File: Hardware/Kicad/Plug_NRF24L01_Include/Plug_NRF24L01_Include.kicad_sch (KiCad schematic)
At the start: 43 parts, among them J1 Conn_01x07_Socket, Q1 2N7002, Q2 2N7002, Q3 2N7002, SW1 SW_Push, U1 NRF24L01, U2 AMS1117-3.3, U3 STM32L412KBTx, Y1 16 MHz

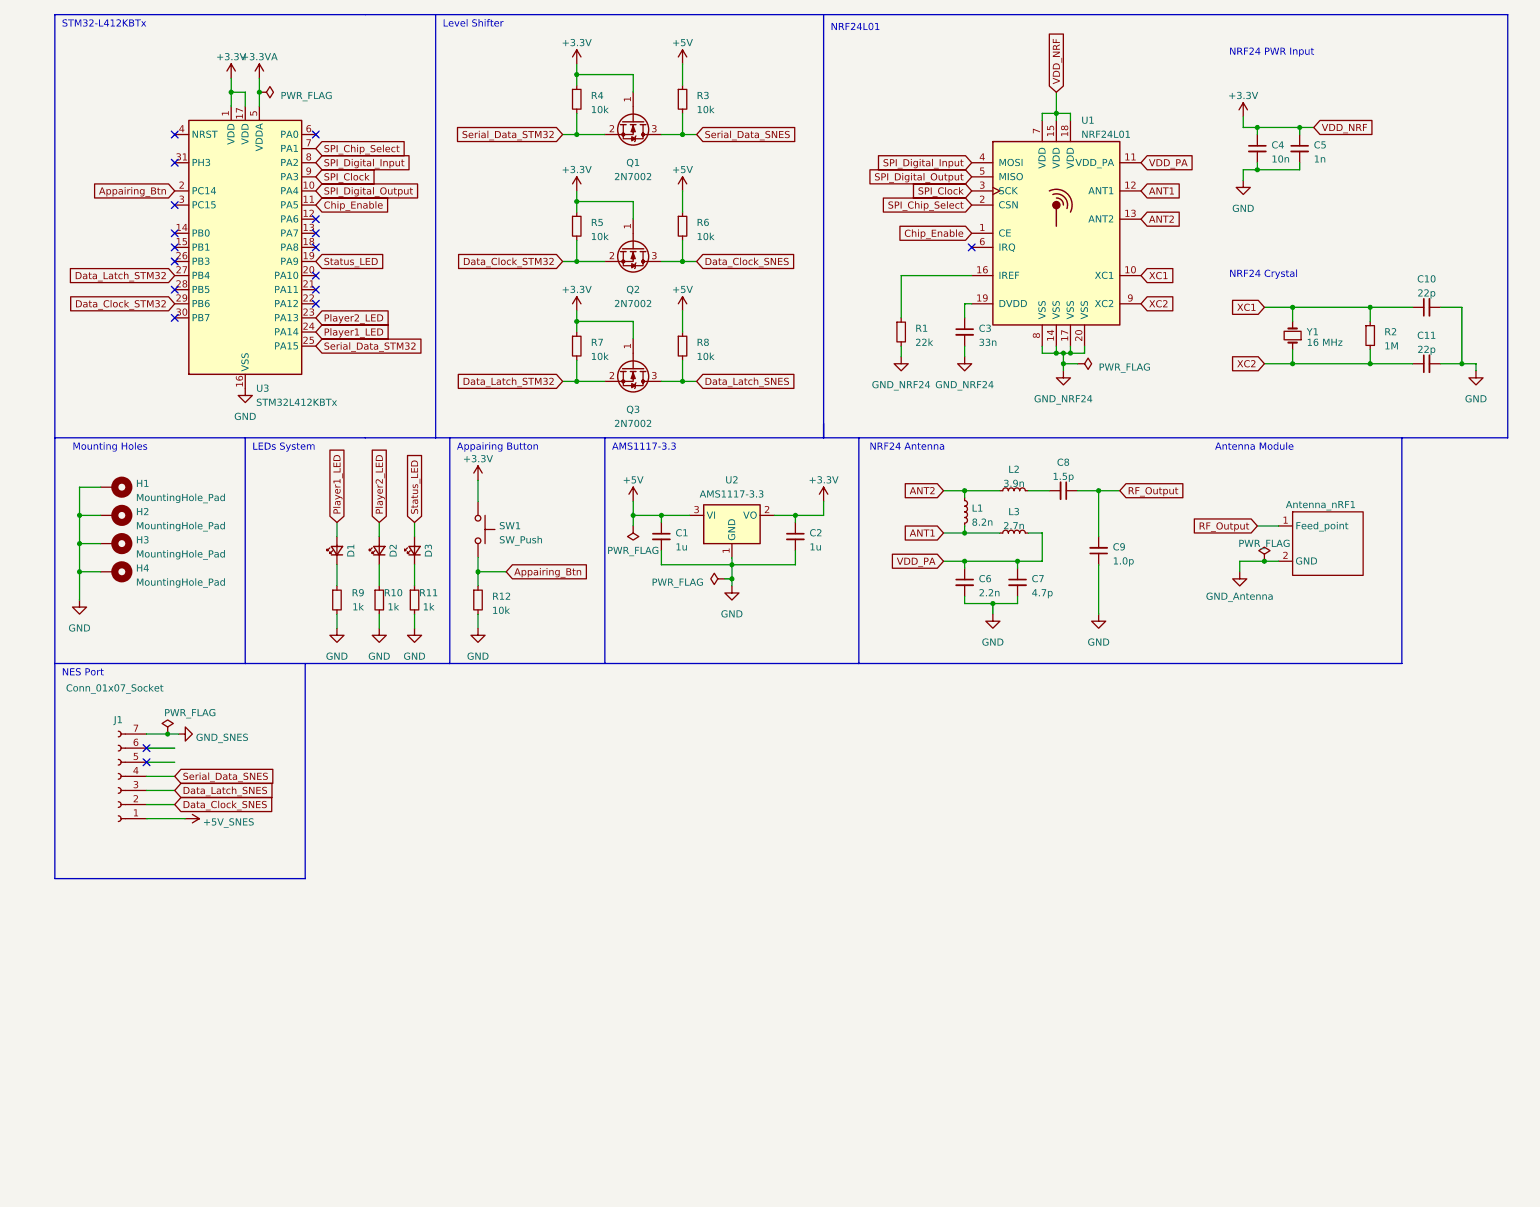
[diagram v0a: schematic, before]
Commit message: Updated NRF24L01_Include
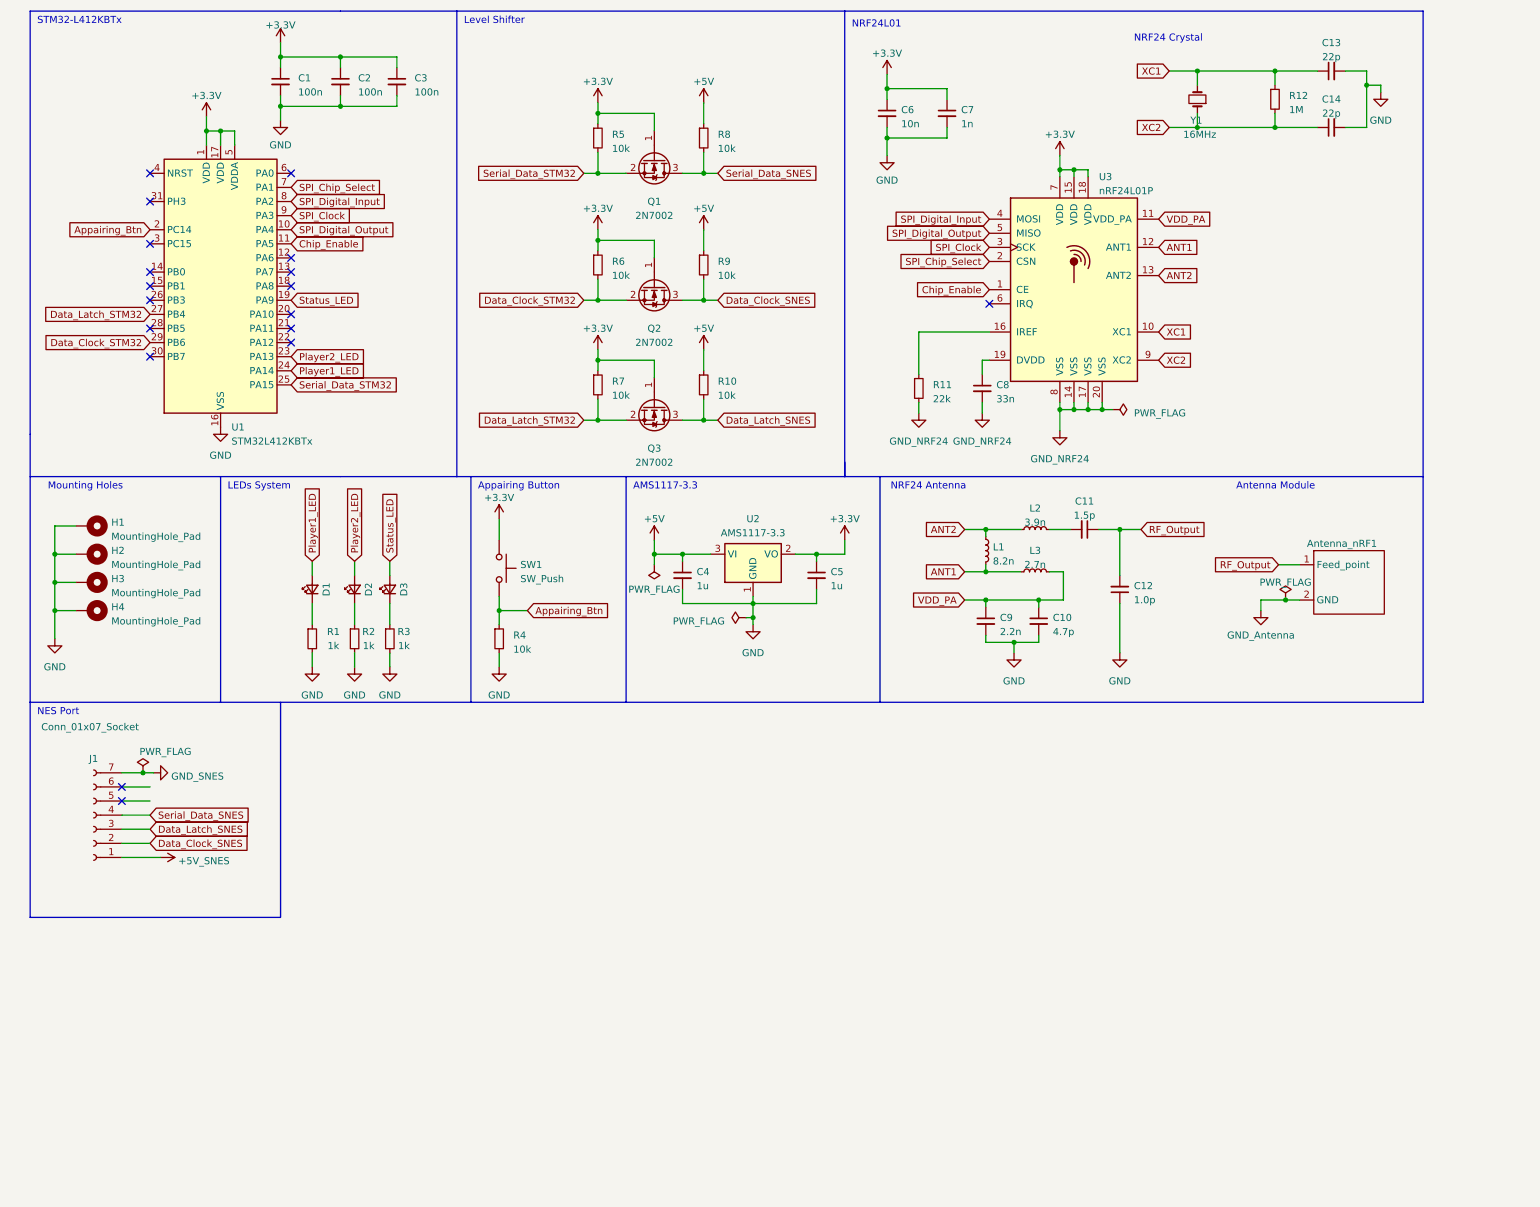
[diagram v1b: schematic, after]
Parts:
- removed C4: 10n, Capacitor_SMD:C_0603_1608Metric_Pad1.08x0.95mm_HandSolder, symbol Device:C_Small
- removed C5: 1n, Capacitor_SMD:C_0603_1608Metric_Pad1.08x0.95mm_HandSolder, symbol Device:C_Small
- removed U1: NRF24L01, Package_DFN_QFN:QFN-20-1EP_4x4mm_P0.5mm_EP2.5x2.5mm, symbol RF:NRF24L01
- added C1, C2, C3: 100n, Capacitor_SMD:C_0603_1608Metric_Pad1.08x0.95mm_HandSolder, symbol Device:C_Small
- added C6: 10n, Capacitor_SMD:C_0603_1608Metric_Pad1.08x0.95mm_HandSolder, symbol Device:C_Small
- added C7: 1n, Capacitor_SMD:C_0603_1608Metric_Pad1.08x0.95mm_HandSolder, symbol Device:C_Small
- added U3: nRF24L01P, Package_DFN_QFN:QFN-20-1EP_4x4mm_P0.5mm_EP2.5x2.5mm, symbol RF:nRF24L01P
- Y1: value 16 MHz -> 16MHz; footprint Crystal:Crystal_HC49-U_Horizontal -> Crystal:Crystal_SMD_HC49-SD_HandSoldering
- renumbered C7 to C10, C8 to C11, C9 to C12, C10 to C13, C11 to C14, C1 to C4, C2 to C5, C3 to C8, C6 to C9, R9 to R1, R8 to R10, R1 to R11, R2 to R12, R10 to R2, R11 to R3, R12 to R4, R4 to R5, R5 to R6, R3 to R8, R6 to R9, U3 to U1
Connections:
- net +3.3VA is gone; now on net +3.3V: U1.5 (VDDA)
- net +3.3V: now also C1.1, C2.1, C3.1, C6.1, C7.1, U3.15 (VDD), U3.18 (VDD), U3.7 (VDD)
- net ANT1: now also U3.12 (ANT1)
- net ANT2: now also U3.13 (ANT2)
- net Chip_Enable: now also U3.1 (CE)
- net GND: now also C1.2, C2.2, C3.2, C6.2, C7.2
- net GND1: now also U3.14 (VSS), U3.17 (VSS), U3.20 (VSS), U3.8 (VSS)
- net SPI_Chip_Select: now also U3.2 (CSN)
- net SPI_Clock: now also U3.3 (SCK)
- net SPI_Digital_Input: now also U3.4 (MOSI)
- net SPI_Digital_Output: now also U3.5 (MISO)
- net VDD_PA: now also U3.11 (VDD_PA)
- net XC1: now also U3.10 (XC1)
- net XC2: now also U3.9 (XC2)
- net at C8.1: now also U3.19 (DVDD)
- net at R11.1: now also U3.16 (IREF)
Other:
- note removed: "NRF24 PWR Input"
- moved on the sheet: Antenna_nRF1, C10, C11, C12, C13, C14, C4, C5, C8, C9, D1, D2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

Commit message: Updated Plug_NRF24L01_Include Schematic & Include (Added new components and modified footprints). Fixed some errors on NRF24L01_Exclude.
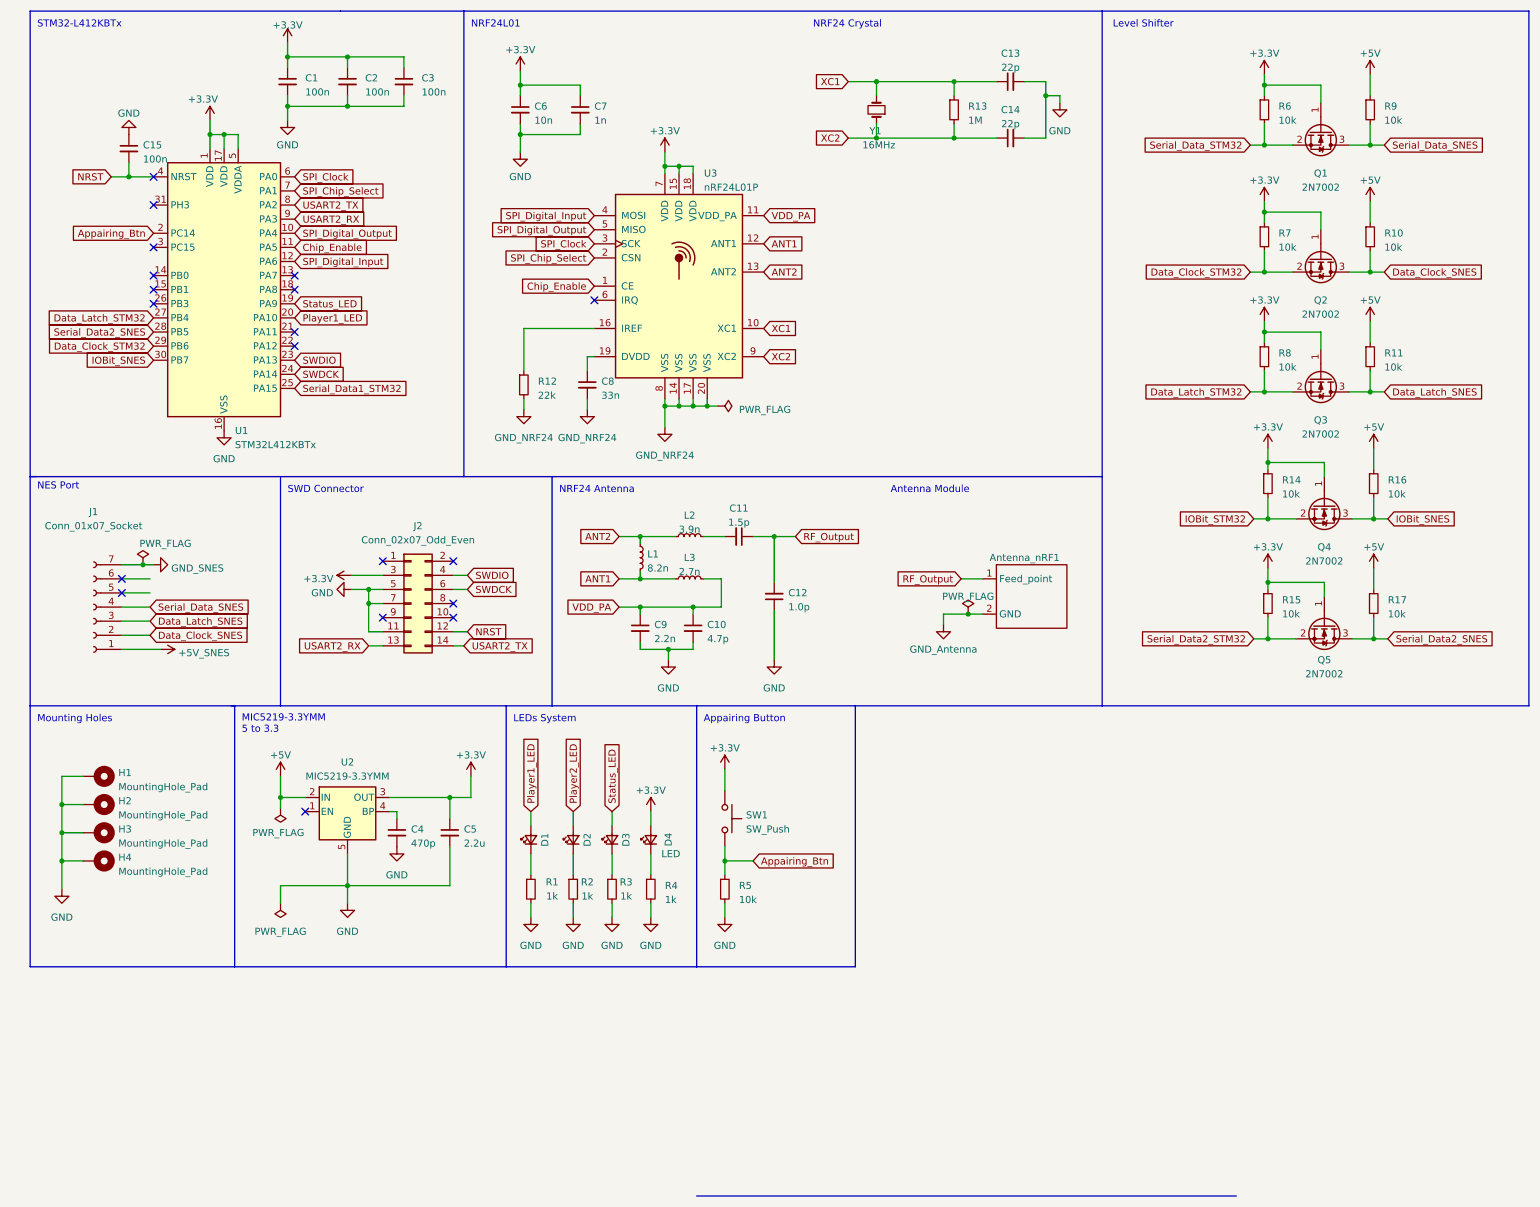
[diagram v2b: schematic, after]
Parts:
- removed U2: AMS1117-3.3, Package_TO_SOT_SMD:SOT-223-3_TabPin2, symbol Regulator_Linear:AMS1117-3.3
- added C15: 100n, Capacitor_SMD:C_0603_1608Metric_Pad1.08x0.95mm_HandSolder, symbol Device:C_Small
- added D4: LED, Diode_SMD:D_0603_1608Metric_Pad1.05x0.95mm_HandSolder, symbol Device:LED_Small
- added J2: Conn_02x07_Odd_Even, Connector_PinHeader_1.27mm:PinHeader_2x07_P1.27mm_Vertical_SMD, symbol Connector_Generic:Conn_02x07_Odd_Even
- added Q4, Q5: 2N7002, Package_TO_SOT_SMD:SOT-23, symbol Transistor_FET:2N7002
- added R14, R15, R16, R17: 10k, Resistor_SMD:R_0603_1608Metric_Pad0.98x0.95mm_HandSolder, symbol Device:R_Small
- added R4: 1k, Resistor_SMD:R_0603_1608Metric_Pad0.98x0.95mm_HandSolder, symbol Device:R_Small
- added U2: MIC5219-3.3YMM, Package_SO:MSOP-8_3x3mm_P0.65mm, symbol Regulator_Linear:MIC5219-3.3YMM
- C4: value 1u -> 470p
- C5: value 1u -> 2.2u
- renumbered R9 to R10, R10 to R11, R11 to R12, R12 to R13, R4 to R5, R5 to R6, R6 to R7, R7 to R8, R8 to R9
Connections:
- net +3.3V: now also D4.2 (A), J2.3 (Pin_3), Q4.1 (G), Q5.1 (G), R14.1, R15.1, U2.3 (OUT)
- net +5V: now also R16.1, R17.1, U2.2 (IN); no longer C4.1
- net GND: now also C15.1, J2.11 (Pin_11), J2.5 (Pin_5), J2.7 (Pin_7), R4.2, U2.5 (GND), U2.6 (GND), U2.7 (GND), U2.8 (GND)
- net Player1_LED: now also U1.20 (PA10); no longer U1.24 (PA14)
- net Player2_LED: no longer U1.23 (PA13)
- net SPI_Clock: now also U1.6 (PA0); no longer U1.9 (PA3)
- net SPI_Digital_Input: now also U1.12 (PA6); no longer U1.8 (PA2)
- net Serial_Data_STM32: no longer U1.25 (PA15)
- net Serial_Data2_SNES: now reaches U1.28 (PB5)
- net Serial_Data2_SNES: now also Q5.3 (D), R17.2
- net IOBit_SNES: now reaches U1.30 (PB7)
- net IOBit_SNES: now also Q4.3 (D), R16.2
- net NRST: now reaches U1.4 (NRST)
- net NRST: now also C15.2, J2.12 (Pin_12)
- new net: D4.1 (K), R4.1
- new net: C4.1, U2.4 (BP)
- new net IOBit_STM32: Q4.2 (S), R14.2
- new net SWDCK: J2.6 (Pin_6), U1.24 (PA14)
- new net SWDIO: J2.4 (Pin_4), U1.23 (PA13)
- new net Serial_Data1_STM32: U1.25 (PA15)
- new net Serial_Data2_STM32: Q5.2 (S), R15.2
- new net USART2_RX: J2.13 (Pin_13), U1.9 (PA3)
- new net USART2_TX: J2.14 (Pin_14), U1.8 (PA2)
- no-connect marks 18 -> 19
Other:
- note added: "MIC5219-3.3YMM 5 to 3.3"
- note added: "SWD Connector"
- note removed: "AMS1117-3.3"
- moved on the sheet: Antenna_nRF1, C1, C10, C11, C12, C13, C14, C2, C3, C6, C7, C8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

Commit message: Updated NRF24L01_Exclude PCB
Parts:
- removed D2: LED_Small, Diode_SMD:D_0603_1608Metric_Pad1.05x0.95mm_HandSolder, symbol Device:LED_Small
- removed R2: 1k, Resistor_SMD:R_0603_1608Metric_Pad0.98x0.95mm_HandSolder, symbol Device:R_Small
- renumbered C15 to C1, C9 to C10, C10 to C11, C11 to C12, C12 to C13, C13 to C14, C14 to C15, C1 to C2, C2 to C3, C3 to C5, C5 to C6, C6 to C7, C7 to C8, C8 to C9, D3 to D2, D4 to D3, R12 to R1, R14 to R10, R15 to R11, R9 to R12, R10 to R13, R11 to R14, R16 to R15, R17 to R16, R1 to R2, R13 to R6, R6 to R7, R7 to R8, R8 to R9
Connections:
- net Serial_Data_STM32 is gone; now on net Serial_Data1_STM32: Q1.2 (S), R7.2
- net IOBit_SNES: now also J1.6 (Pin_6); no longer U1.30 (PB7)
- net IOBit_STM32: now also U1.30 (PB7)
- net Serial_Data2_SNES: now also J1.5 (Pin_5); no longer U1.28 (PB5)
- net Serial_Data2_STM32: now also U1.28 (PB5)
- net Serial_Data_SNES renamed Serial_Data1_SNES
- no-connect marks 19 -> 17
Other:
- moved on the sheet: C6, D2, D3, R3, R4, R5, SW1

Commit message: Updated PCB (Grouping and Tracks)
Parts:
- J1: footprint Connector_PinSocket_1.00mm:PinSocket_1x07_P1.00mm_Vertical -> Connector_JST:JST_EH_B7B-EH-A_1x07_P2.50mm_Vertical
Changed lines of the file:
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@@
       (effects (font (size 1.27 1.27)))
     )
-    (property "Footprint" "Connector_PinSocket_1.00mm:PinSocket_1x07_P1.00mm_Vertical" (at 24.765 120.65 0)
+    (property "Footprint" "Connector_JST:JST_EH_B7B-EH-A_1x07_P2.50mm_Vertical" (at 24.765 120.65 0)
       (effects (font (size 1.27 1.27)) hide)
     )
